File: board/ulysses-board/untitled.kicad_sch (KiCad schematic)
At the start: 49 parts, among them J5 I2C_3V3, Q10 BC548, Q11 BC548, Q12 BC548, Q13 BC548, Q14 BC548, Q4 BC548, Q5 BC548, Q6 BC548, Q7 BC548, Q8 BC548, Q9 BC548, SW11 TAMP_DET, SW12 TAMP_DET, SW13 TAMP_DET2, SW14 TAMP_DET2, U10 EVENT_MEM, U11 EEPROM_3V3, U9 MCP23008

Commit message: Make some minor fixes.
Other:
- note added: "Tamper detection / Status"
- note removed: "Tamper detection / Alert"
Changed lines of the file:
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@@
     (rev "1.2")
     (company "Dirk Gottschalk")
-    (comment 1 "Alert / I2C module")
+    (comment 1 "Status & I2C module")
     (comment 2 "Schematics")
     (comment 3 "Draft")
@@
     (effects (font (size 3.81 3.81)) (justify left bottom))
   )
-  (text "Tamper detection / Alert" (at 105.41 21.59 0)
+  (text "Tamper detection / Status" (at 105.41 21.59 0)
     (effects (font (size 3.81 3.81)) (justify left bottom))
   )
-  (text "I²C EEPROM R/W\n I²C breakout" (at 101.6 113.03 0)
+  (text "I²C EEPROM R/W\n  I²C breakout" (at 101.6 113.03 0)
     (effects (font (size 3.81 3.81)) (justify left bottom))
   )

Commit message: Add a real-time clock.
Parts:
- added BT1: CR2032, Battery:BatteryHolder_Keystone_1058_1x2032, symbol Device:Battery_Cell
- added C18, C19, C20, C23: 100nF, symbol Device:C
- added C21, C22: 10pF, symbol Device:C
- added D11: LED, symbol Device:LED
- added R33: 330, symbol Device:R
- added U12: MCP7940N-xP, Package_DIP:DIP-8_W7.62mm_Socket_LongPads, symbol Timer_RTC:MCP7940N-xP
- added Y1: 32.768kHz, symbol Device:Crystal
- renumbered D11 to D12, R21 to R19, R22 to R20, R23 to R21, R24 to R22, R25 to R23, R26 to R24, R27 to R25, R28 to R26, R29 to R27, R30 to R28, R31 to R29, R32 to R30, R33 to R31, R34 to R32, R35 to R34, R36 to R35, R37 to R36, R38 to R37, R39 to R38, R40 to R39, R41 to R40, R42 to R41
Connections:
- net +3V3: now also C18.1, C19.1, C20.2, C23.1, U12.8 (VCC)
- net GNDD: now also BT1.2 (-), C18.2, C19.2, C20.1, C21.2, C22.2, C23.2, D11.1 (K), U12.4 (VSS)
- net GPIO[2]/SDA1: now also U12.5 (SDA)
- net GPIO[3]/SCL1: now also U12.6 (SCL)
- new net: C22.1, U12.2 (X2), Y1.1
- new net: C21.1, U12.1 (X1), Y1.2
- new net: D11.2 (A), R33.1
- new net: R33.2, U12.7 (MFP)
- new net: BT1.1 (+), U12.3 (VBAT)
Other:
- note added: "RTC (real-time clock)"

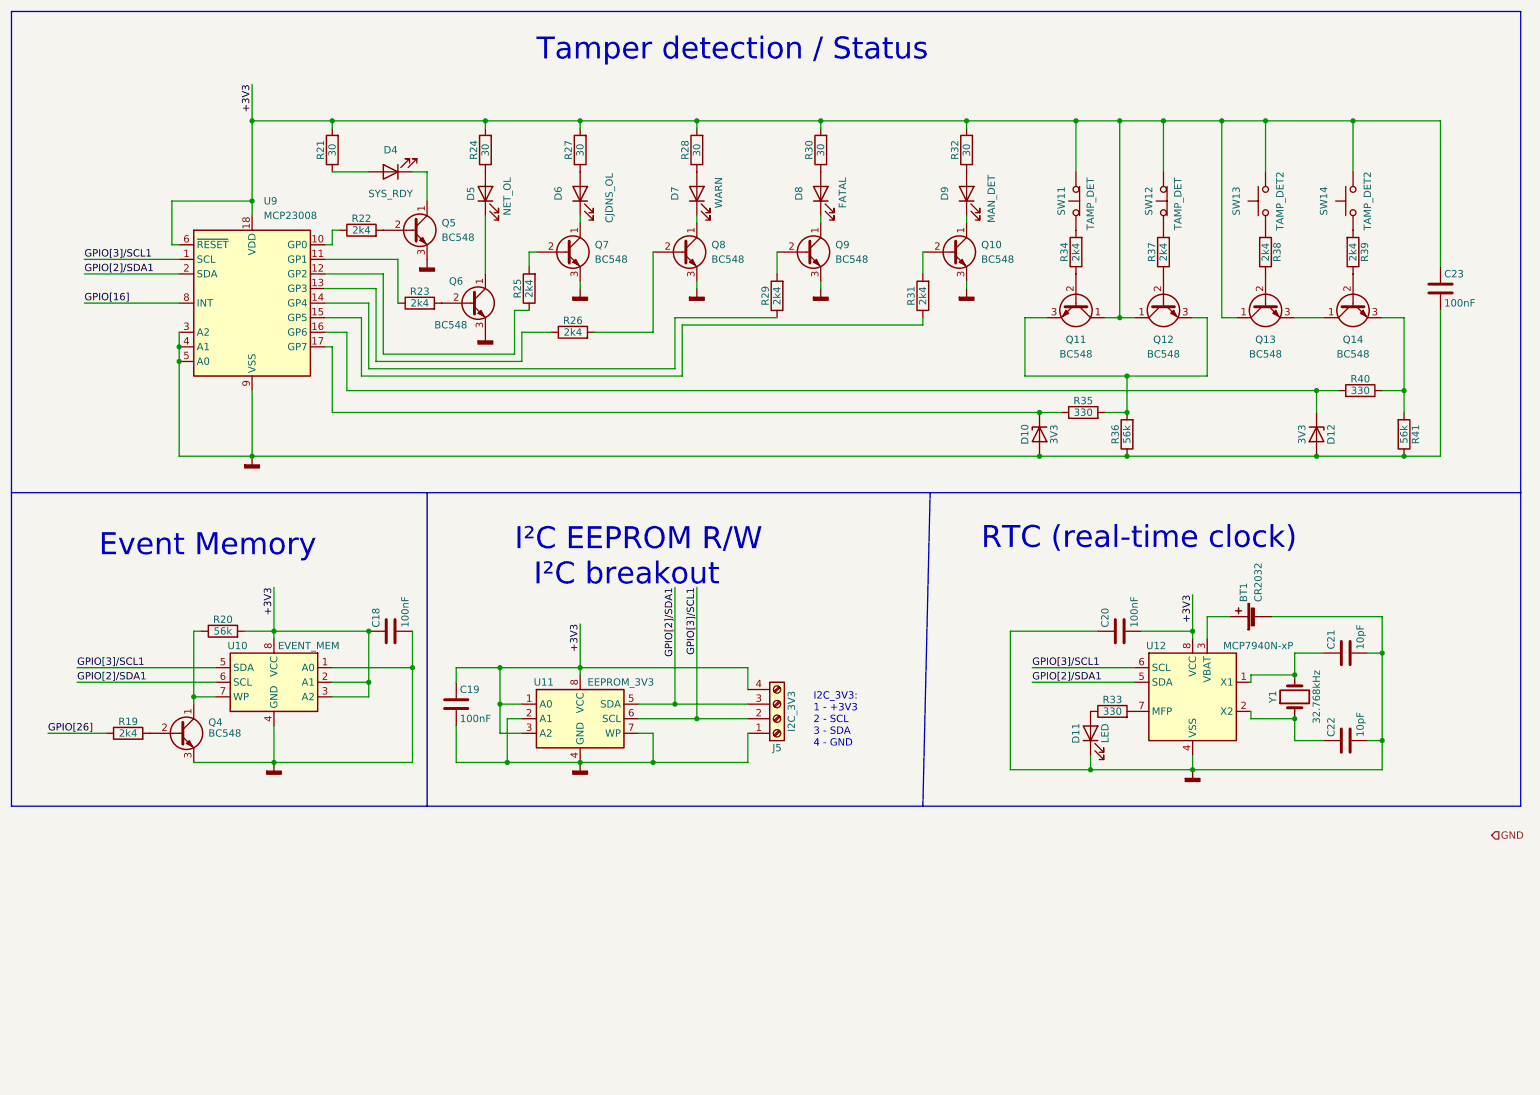
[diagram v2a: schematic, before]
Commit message: Make schemaics more readable.
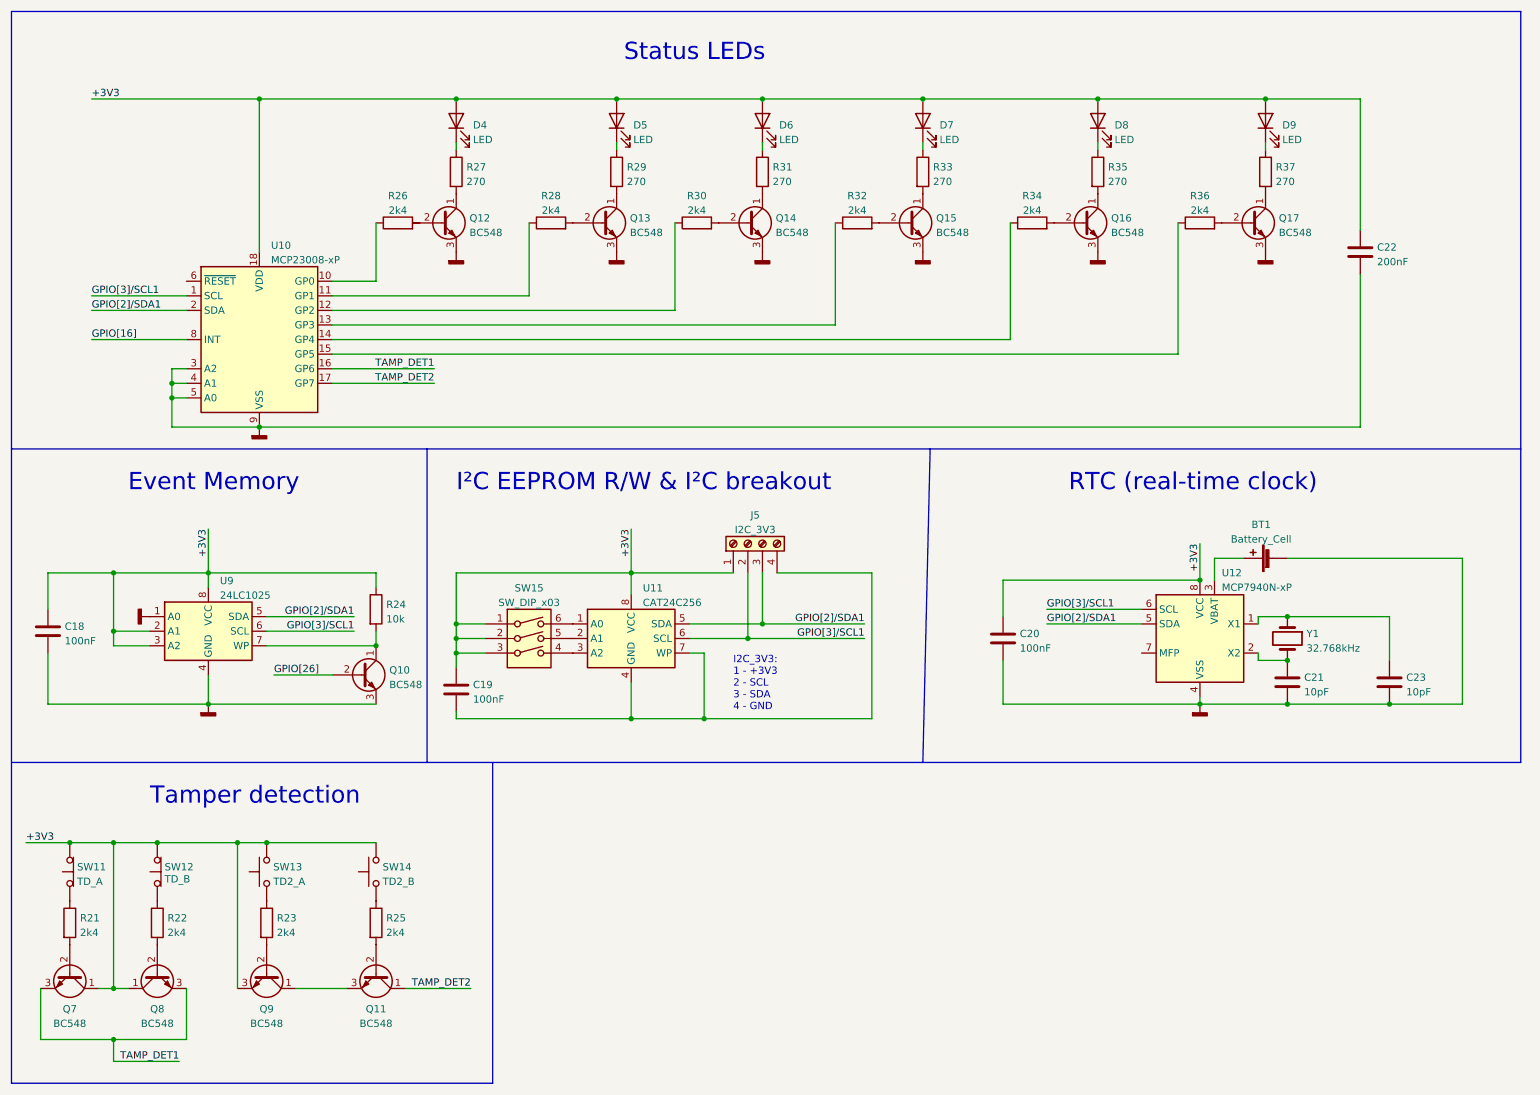
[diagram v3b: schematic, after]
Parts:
- removed D10, D12: 3V3, symbol Device:D_Zener
- removed D11: LED, symbol Device:LED
- removed Q4, Q5, Q6: BC548, Package_TO_SOT_THT:TO-92_Inline, symbol Transistor_BJT:BC548
- removed R19, R38, R39: 2k4, symbol Device:R
- removed R20, R41: 56k, symbol Device:R
- removed R40: 330, symbol Device:R
- removed U10: EVENT_MEM, symbol Memory_EEPROM:24LC1025
- removed U11: EEPROM_3V3, Package_DIP:DIP-8_W7.62mm_Socket_LongPads, symbol Memory_EEPROM:24LC1025
- removed U9: MCP23008, Package_DIP:DIP-18_W7.62mm, symbol Interface_Expansion:MCP23008-xP
- added Q15, Q16, Q17: BC548, Package_TO_SOT_THT:TO-92_Inline, symbol Transistor_BJT:BC548
- added SW15: SW_DIP_x03, symbol Switch:SW_DIP_x03
- added U10: MCP23008-xP, Package_DIP:DIP-18_W7.62mm, symbol Interface_Expansion:MCP23008-xP
- added U11: CAT24C256, symbol Memory_EEPROM:CAT24C256
- added U9: 24LC1025, symbol Memory_EEPROM:24LC1025
- BT1: value CR2032 -> Battery_Cell; footprint Battery:BatteryHolder_Keystone_1058_1x2032 -> (none)
- C22: value 10pF -> 200nF
- C23: value 100nF -> 10pF
- D4: value SYS_RDY -> LED; footprint LED_THT:LED_D3.0mm_Horizontal_O1.27mm_Z10.0mm -> (none)
- D5: value NET_OL -> LED; footprint LED_THT:LED_D3.0mm_Horizontal_O1.27mm_Z10.0mm -> (none)
- D6: value CJDNS_OL -> LED; footprint LED_THT:LED_D3.0mm_Horizontal_O1.27mm_Z10.0mm -> (none)
- D7: value WARN -> LED; footprint LED_THT:LED_D3.0mm_Horizontal_O1.27mm_Z10.0mm -> (none)
- D8: value FATAL -> LED; footprint LED_THT:LED_D3.0mm_Horizontal_O1.27mm_Z10.0mm -> (none)
- D9: value MAN_DET -> LED; footprint LED_THT:LED_D3.0mm_Horizontal_O1.27mm_Z10.0mm -> (none)
- R21, R28, R30, R32: value 30 -> 2k4
- R24: value 30 -> 10k
- R27: value 30 -> 270
- R29, R31, R37: value 2k4 -> 270
- R33, R35: value 330 -> 270
- R36: value 56k -> 2k4
- SW11: value TAMP_DET -> TD_A
- SW12: value TAMP_DET -> TD_B
- SW13: value TAMP_DET2 -> TD2_A
- SW14: value TAMP_DET2 -> TD2_B
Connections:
- net +3V3: now also C20.1, C22.1, D4.2 (A), D5.2 (A), D6.2 (A), D7.2 (A), D8.2 (A), D9.2 (A), J5.1 (Pin_1), Q7.1 (C), Q8.1 (C), Q9.3 (E), R24.1, SW15.1, SW15.2, SW15.3, U10.18 (VDD), U11.8 (VCC), U9.2 (A1), U9.3 (A2), U9.8 (VCC); no longer C20.2, C23.1, J5.4 (Pin_4), Q11.1 (C), Q12.1 (C), Q13.1 (C), R21.2, R24.2, R27.2, R28.2, R30.2, R32.2
- net GNDD: now also C20.2, Q12.3 (E), Q13.3 (E), Q14.3 (E), Q15.3 (E), Q16.3 (E), Q17.3 (E), U10.3 (A2), U10.4 (A1), U10.5 (A0), U10.9 (VSS), U9.1 (A0), U9.4 (GND); no longer C19.2, C20.1, J5.1 (Pin_1), Q7.3 (E), Q8.3 (E), Q9.3 (E), R36.1
- net GPIO[16]: now also U10.8 (INT)
- net GPIO[26]: now also Q10.2 (B)
- net GPIO[2]/SDA1: now also U10.2 (SDA), U11.5 (SDA), U9.5 (SDA)
- net GPIO[3]/SCL1: now also U10.1 (SCL), U11.6 (SCL), U9.6 (SCL)
- net at Q10.1 (C): now also R24.2, U9.7 (WP); no longer D9.1 (K)
- net at R31.2: now also Q14.1 (C); no longer Q10.2 (B)
- net at C21.1, Y1.2: now also U12.2 (X2); no longer U12.1 (X1)
- net at R32.1: now also U10.13 (GP3); no longer D9.2 (A)
- net at R22.1: now also SW12.1 (A)
- net at R23.1: now also SW13.1
- net at R25.1: now also SW14.1
- net at R26.1: now also U10.10 (GP0)
- net at R29.1: now also D5.1 (K)
- net at R31.1: now also D6.1 (K)
- net at R35.1: now also D8.1 (K)
- net at R33.1: now also D7.1 (K)
- net at R33.2: now also Q15.1 (C); no longer U12.7 (MFP)
- net at Q12.2 (B): no longer R37.1
- net at R37.2: now also Q17.1 (C); no longer SW12.1 (A)
- net at Q8.2 (B): now also R22.2; no longer R26.2
- net at R34.1: now also U10.14 (GP4); no longer Q11.2 (B)
- net at R34.2: now also Q16.2 (B); no longer SW11.1 (A)
- net at Q14.2 (B): now also R30.2
- net at Q13.2 (B): now also R28.2
- net at R27.1: now also D4.1 (K); no longer D6.2 (A)
- net at R28.1: now also U10.11 (GP1); no longer D7.2 (A)
- net at R21.1: now also SW11.1 (A); no longer D4.2 (A)
- net at R25.2: now also Q11.2 (B); no longer Q7.2 (B)
- net at Q9.2 (B): now also R23.2; no longer R29.2
- net at Q9.1 (C): now also Q11.3 (E); no longer D8.1 (K)
- net at R30.1: now also U10.12 (GP2); no longer D8.2 (A)
- new net: Q17.2 (B), R36.2
- new net: SW15.6, U11.1 (A0)
- new net: SW15.5, U11.2 (A1)
- new net: SW15.4, U11.3 (A2)
- new net: C19.2, J5.4 (Pin_4), U11.4 (GND), U11.7 (WP)
- new net: Q15.2 (B), R32.2
- new net: Q7.2 (B), R21.2
- new net: Q16.1 (C), R35.2
- new net: Q12.1 (C), R27.2
- new net: Q13.1 (C), R29.2
- new net: C23.1, U12.1 (X1), Y1.1
- new net: R36.1, U10.15 (GP5)
- new net: D9.1 (K), R37.1
- new net TAMP_DET1: Q7.3 (E), Q8.3 (E), U10.16 (GP6)
- new net TAMP_DET2: Q11.1 (C), U10.17 (GP7)
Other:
- note added: "I²C EEPROM R/W & I²C breakout"
- note added: "Status LEDs"
- note added: "Tamper detection"
- note removed: "I²C EEPROM R/W I²C breakout"
- note removed: "Tamper detection / Status"

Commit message: Some minor imptovements.
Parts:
- BT1: value Battery_Cell -> CR2032
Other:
- moved on the sheet: C18, C19, J5, Q10, R24, SW15, U11, U9
